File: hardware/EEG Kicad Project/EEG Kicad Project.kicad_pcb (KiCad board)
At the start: 2 copper layers, 1 part, among them U1 STM32F446RETx

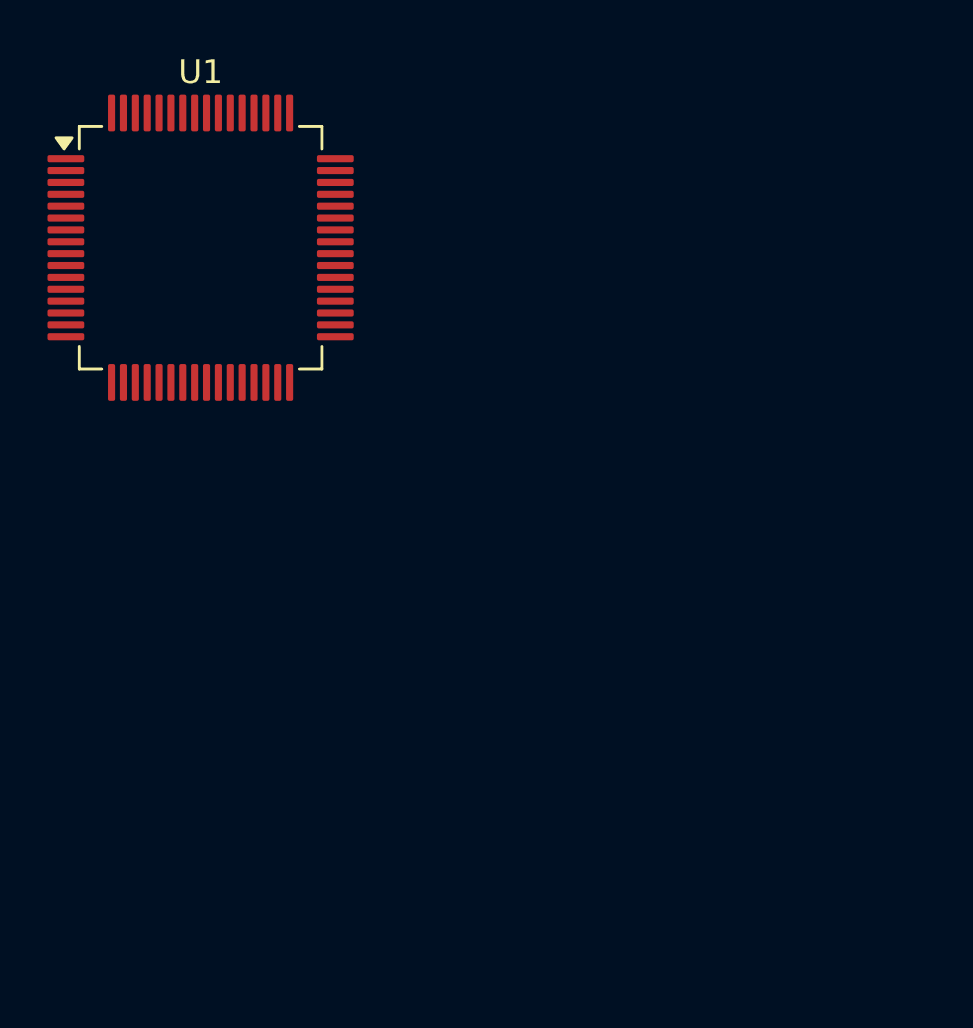
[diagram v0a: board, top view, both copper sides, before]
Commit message: Added datasheet, modify STM32 pinout in MX, added labels on schematic, added STM32 hierarch sheet
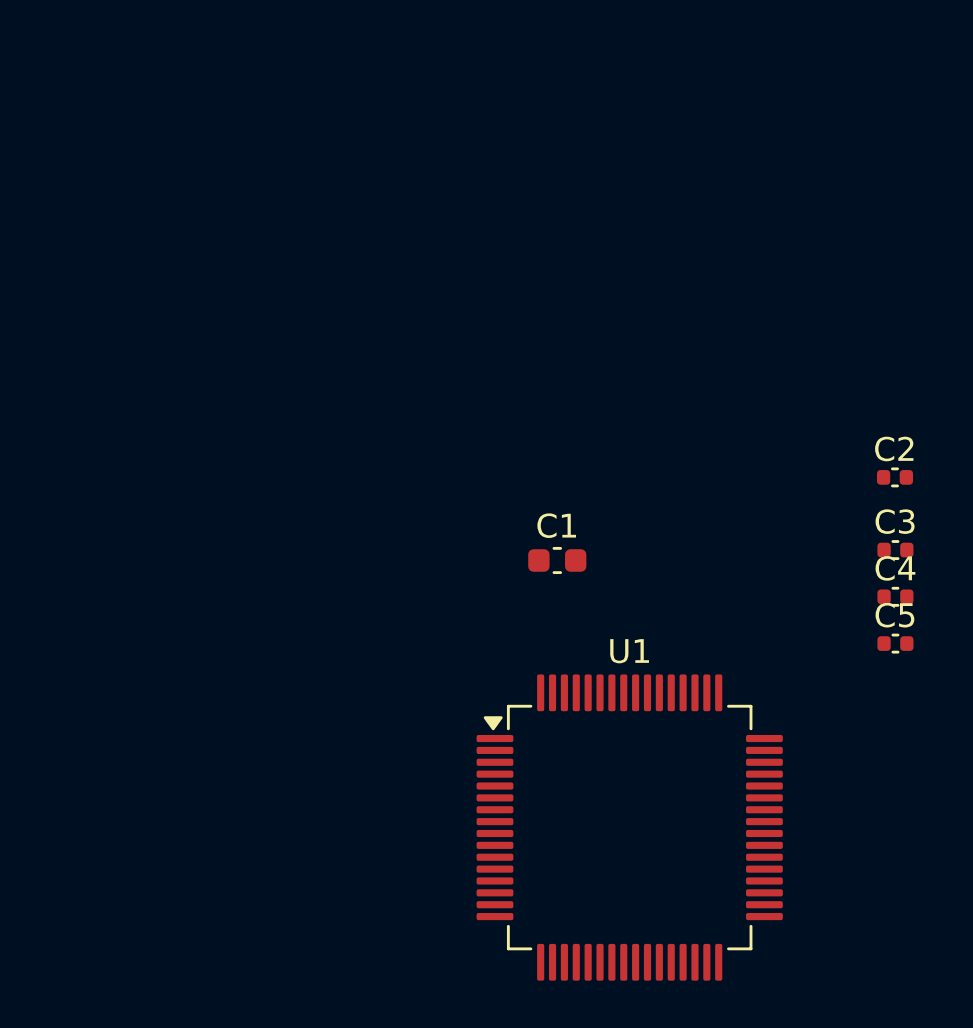
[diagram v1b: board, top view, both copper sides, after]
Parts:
- added C1: 1u, Capacitor_SMD:C_0603_1608Metric, F.Cu at (85.8, 64.0)
- added C2: 100n, Capacitor_SMD:C_0402_1005Metric, F.Cu at (100.0, 60.5)
- added C3: 100n, Capacitor_SMD:C_0402_1005Metric, F.Cu at (100.0, 63.6)
- added C4: 100n, Capacitor_SMD:C_0402_1005Metric, F.Cu at (100.0, 65.5)
- added C5: 100n, Capacitor_SMD:C_0402_1005Metric, F.Cu at (100.0, 67.5)
- moved U1 30.4 mm to (88.8, 75.2)
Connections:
- U1 pad 19: unconnected-(U1-VDD-Pad19) -> +3V3
- U1 pad 32: unconnected-(U1-VDD-Pad32) -> +3V3
- U1 pad 48: unconnected-(U1-VDD-Pad48) -> +3V3
- U1 pad 64: unconnected-(U1-VDD-Pad64) -> +3V3
